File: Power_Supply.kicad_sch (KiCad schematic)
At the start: 22 parts, among them J1 12V_Input, U1 TPS54360DDA, U2 AMS1117-3.3

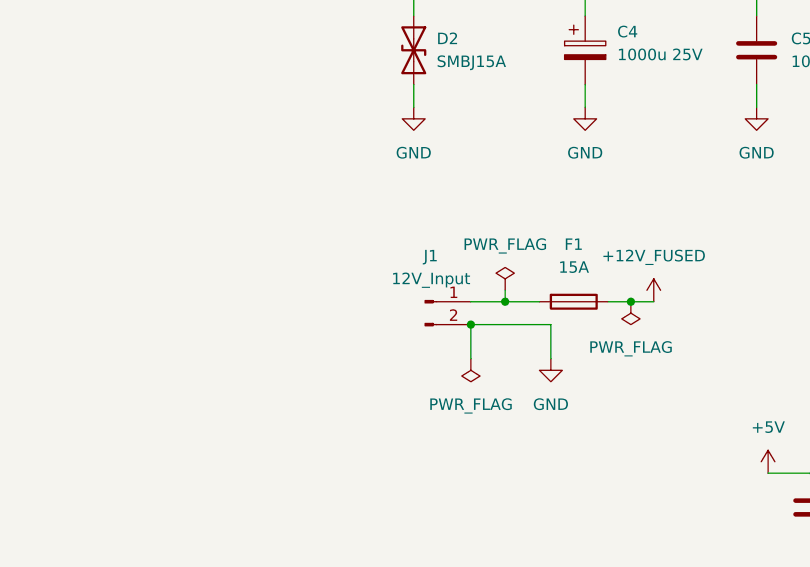
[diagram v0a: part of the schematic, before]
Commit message: Updated traces on PCB for the power supply, added XT60PW power connector for the board.
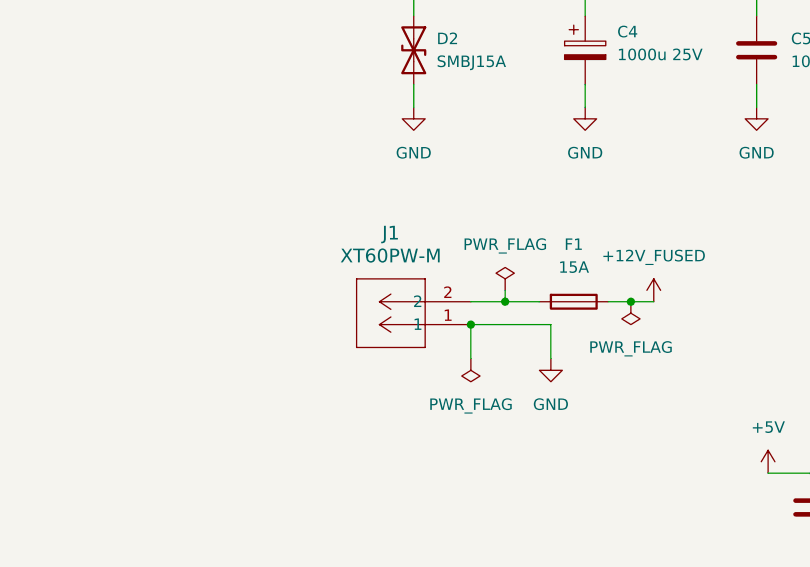
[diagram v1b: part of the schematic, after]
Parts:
- removed J1: 12V_Input, Connector_PinSocket_2.00mm:PinSocket_1x02_P2.00mm_Horizontal, symbol Connector:Conn_01x02_Pin
- added J1: XT60PW-M, CONN_XT60PW-M_AMA, symbol Stepper_ESC:XT60PW-M
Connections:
- net GND: now also J1.1
- net at F1.2: now also J1.2
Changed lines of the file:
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@@
 	)
 	(junction
-		(at 85.09 55.88)
+		(at 67.31 58.42)
 		(diameter 0)
 		(color 0 0 0 0)
 	)
 	(junction
-		(at 163.83 22.86)
+		(at 85.09 55.88)
 		(diameter 0)
 		(color 0 0 0 0)
 	)
 	(junction
-		(at 163.83 38.1)
+		(at 163.83 22.86)
 		(diameter 0)
 		(color 0 0 0 0)
 	)
 	(junction
-		(at 185.42 36.83)
+		(at 163.83 38.1)
 		(diameter 0)
 		(color 0 0 0 0)
 	)
 	(junction
-		(at 67.31 58.42)
+		(at 185.42 36.83)
 		(diameter 0)
 		(color 0 0 0 0)
@@
 	)
 	(symbol
-		(lib_id "Connector:Conn_01x02_Pin")
-		(at 62.23 55.88 0)
-		(unit 1)
-		(body_style 1)
-		(exclude_from_sim no)
-		(in_bom yes)
-		(on_board yes)
-		(in_pos_files yes)
-		(dnp no)
-		(fields_autoplaced yes)
-		(property "Reference" "J1"
-			(at 62.865 50.8 0)
-			(show_name no)
-			(do_not_autoplace no)
-			(effects
-				(font
-					(size 1.27 1.27)
-				)
-			)
-		)
-		(property "Value" "12V_Input"
-			(at 62.865 53.34 0)
-			(show_name no)
-			(do_not_autoplace no)
-			(effects
-				(font
-					(size 1.27 1.27)
-				)
-			)
-		)
-		(property "Footprint" "Connector_PinSocket_2.00mm:PinSocket_1x02_P2.00mm_Horizontal"
-			(at 62.23 55.88 0)
-			(hide yes)
-			(show_name no)
-			(do_not_autoplace no)
-			(effects
-				(font
-					(size 1.27 1.27)
-				)
-			)
-		)
-		(property "Datasheet" ""
-			(at 62.23 55.88 0)
-			(hide yes)
-			(show_name no)
-			(do_not_autoplace no)
-			(effects
-				(font
-					(size 1.27 1.27)
-				)
-			)
-		)
-		(property "Description" "Generic connector, single row, 01x02, script generated"
-			(at 62.23 55.88 0)
-			(hide yes)
-			(show_name no)
-			(do_not_autoplace no)
-			(effects
-				(font
-					(size 1.27 1.27)
-				)
-			)
-		)
-		(pin "2"
-		)
-		(pin "1"
-		)
-		(instances
-			(project "Stepper_ESC"
-				(path "/9271e9dc-3850-4149-b59f-a263c29a5edc/588db524-0e83-4bd4-9197-9ff33ddc086a"
-					(reference "J1")
-					(unit 1)
-				)
-			)
-		)
-	)
-	(symbol
 		(lib_id "power:GND")
 		(at 194.31 58.42 0)
@@
 					(unit 1)
 				)
+			)
+		)
+	)
+	(symbol
+		(lib_id "Stepper_ESC:XT60PW-M")
+		(at 67.31 58.42 180)
+		(unit 1)
+		(body_style 1)
+		(exclude_from_sim no)
+		(in_bom yes)
+		(on_board yes)
+		(in_pos_files yes)
+		(dnp no)
+		(fields_autoplaced yes)
+		(property "Reference" "J1"
+			(at 58.42 48.26 0)
+			(show_name no)
+			(do_not_autoplace no)
+			(effects
+				(font
+					(size 1.524 1.524)
+				)
+			)
+		)
+		(property "Value" "XT60PW-M"
+			(at 58.42 50.8 0)
+			(show_name no)
+			(do_not_autoplace no)
+			(effects
+				(font
+					(size 1.524 1.524)
+				)
+			)
+		)
+		(property "Footprint" "CONN_XT60PW-M_AMA"
+			(at 65.024 66.548 0)
+			(hide yes)
+			(show_name no)
+			(do_not_autoplace no)
+			(effects
+				(font
+					(size 1.27 1.27)
+					(italic yes)
+				)
+			)
+		)
+		(property "Datasheet" "XT60PW-M"
+			(at 70.358 64.516 0)
+			(hide yes)
+			(show_name no)
+			(do_not_autoplace no)
+			(effects
+				(font
+					(size 1.27 1.27)
+					(italic yes)
+				)
+			)
+		)
+		(property "Description" ""
+			(at 67.31 58.42 0)
+			(hide yes)
+			(show_name no)
+			(do_not_autoplace no)
+			(effects
+				(font
+					(size 1.27 1.27)
+				)
+			)
+		)
+		(pin "1"
+		)
+		(pin "2"
+		)
+		(instances
+			(project "Stepper_ESC"
+				(path "/9271e9dc-3850-4149-b59f-a263c29a5edc/588db524-0e83-4bd4-9197-9ff33ddc086a"
+					(reference "J1")
+					(unit 1)
+				)

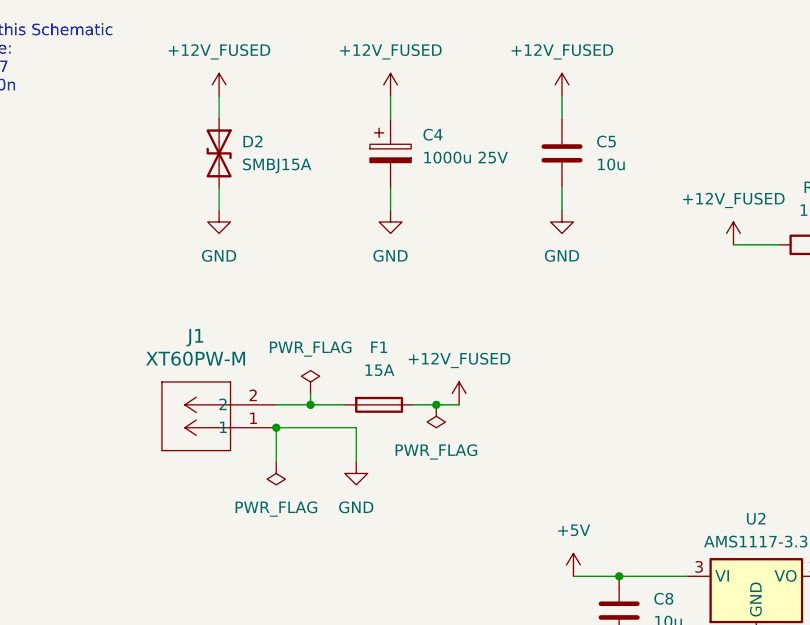
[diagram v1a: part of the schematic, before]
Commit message: Added Fuse holder and diode footprints
Signed-off-by: Vincent Cadicamo <vcadicamo@icloud.com>
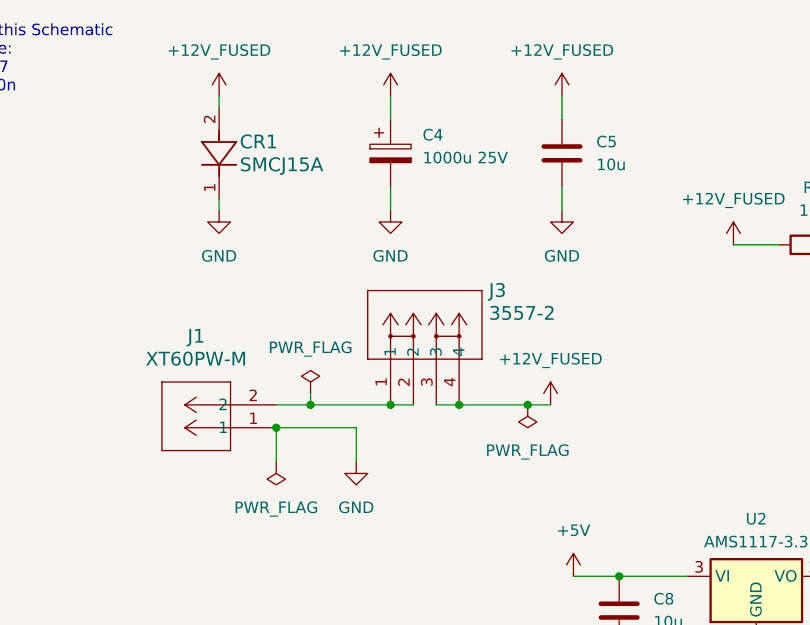
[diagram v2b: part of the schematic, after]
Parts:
- removed D2: SMBJ15A, Diode_SMD:D_01005_0402Metric, symbol Device:D_TVS
- removed F1: 15A, Fuse:Fuse_0402_1005Metric, symbol Device:Fuse
- added CR1: SMCJ15A, DIODE_DO-214AC, symbol Stepper_ESC:SMCJ15A
- added J3: 3557-2, CONN_3557-2_KEY, symbol Stepper_ESC:3557-2
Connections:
- net +12V_FUSED: now also CR1.2, J3.3, J3.4
- net GND: now also CR1.1
- net at J1.2: now also J3.1, J3.2
